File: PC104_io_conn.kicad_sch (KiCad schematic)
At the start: 1 part, among them P14 Conn_04x26_Pin

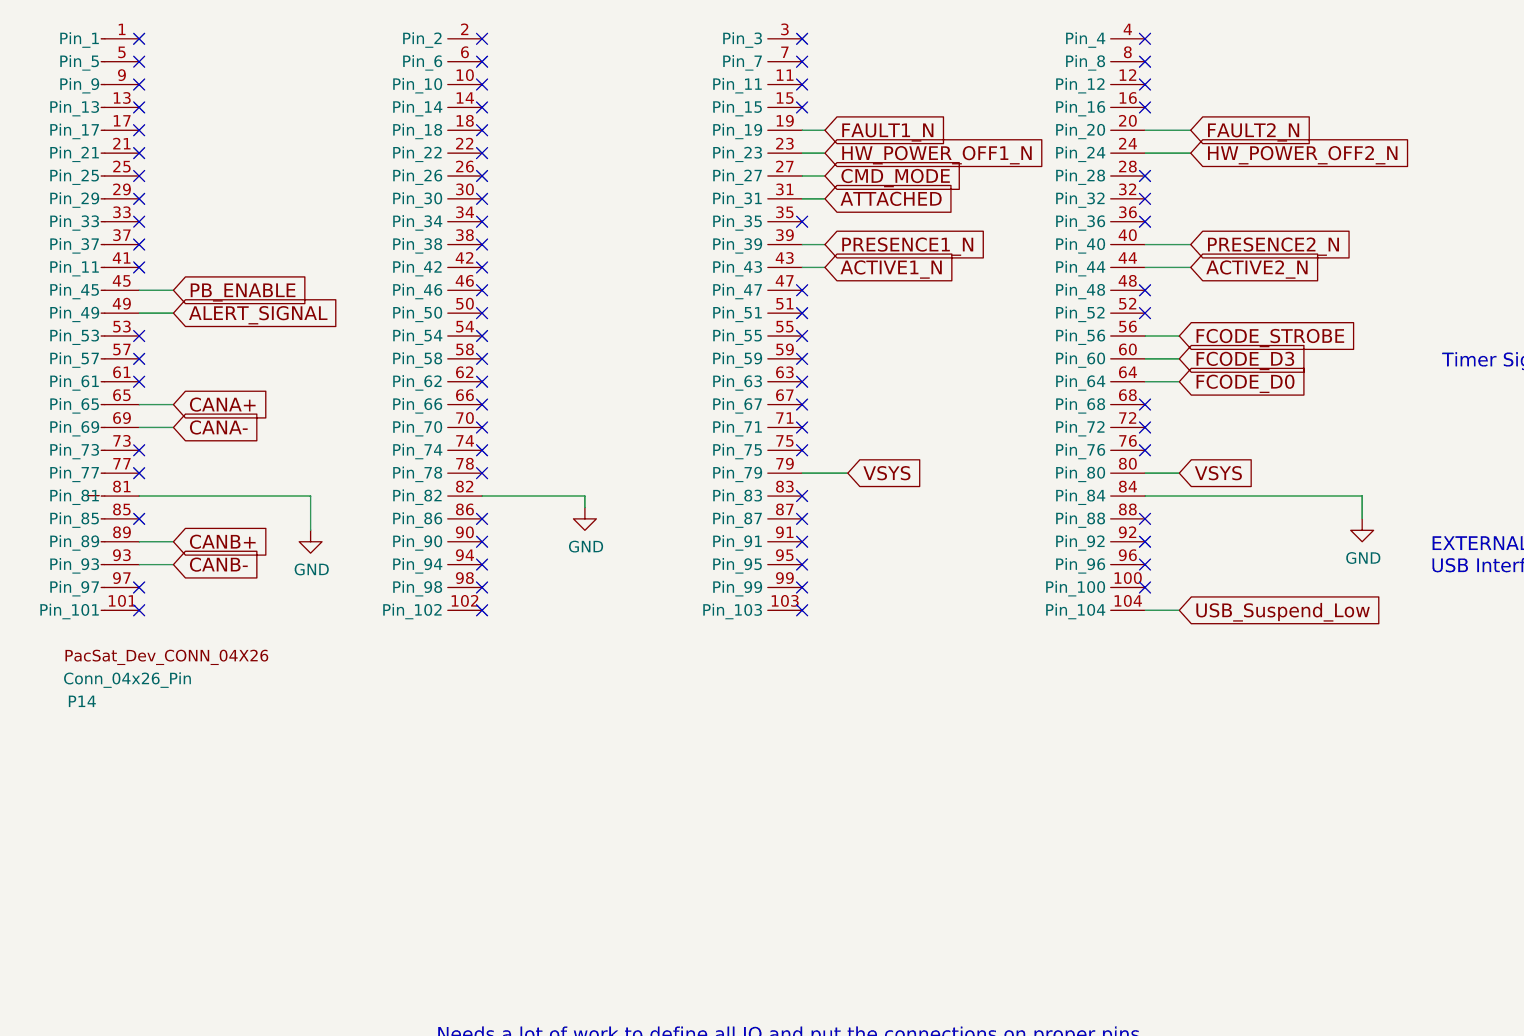
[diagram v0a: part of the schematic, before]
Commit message: Do a ton of work to switch to the CubeSat Kit Bus
Redo the connector, board shape, etc.

Signed-off-by: Corey Minyard <corey@minyard.net>
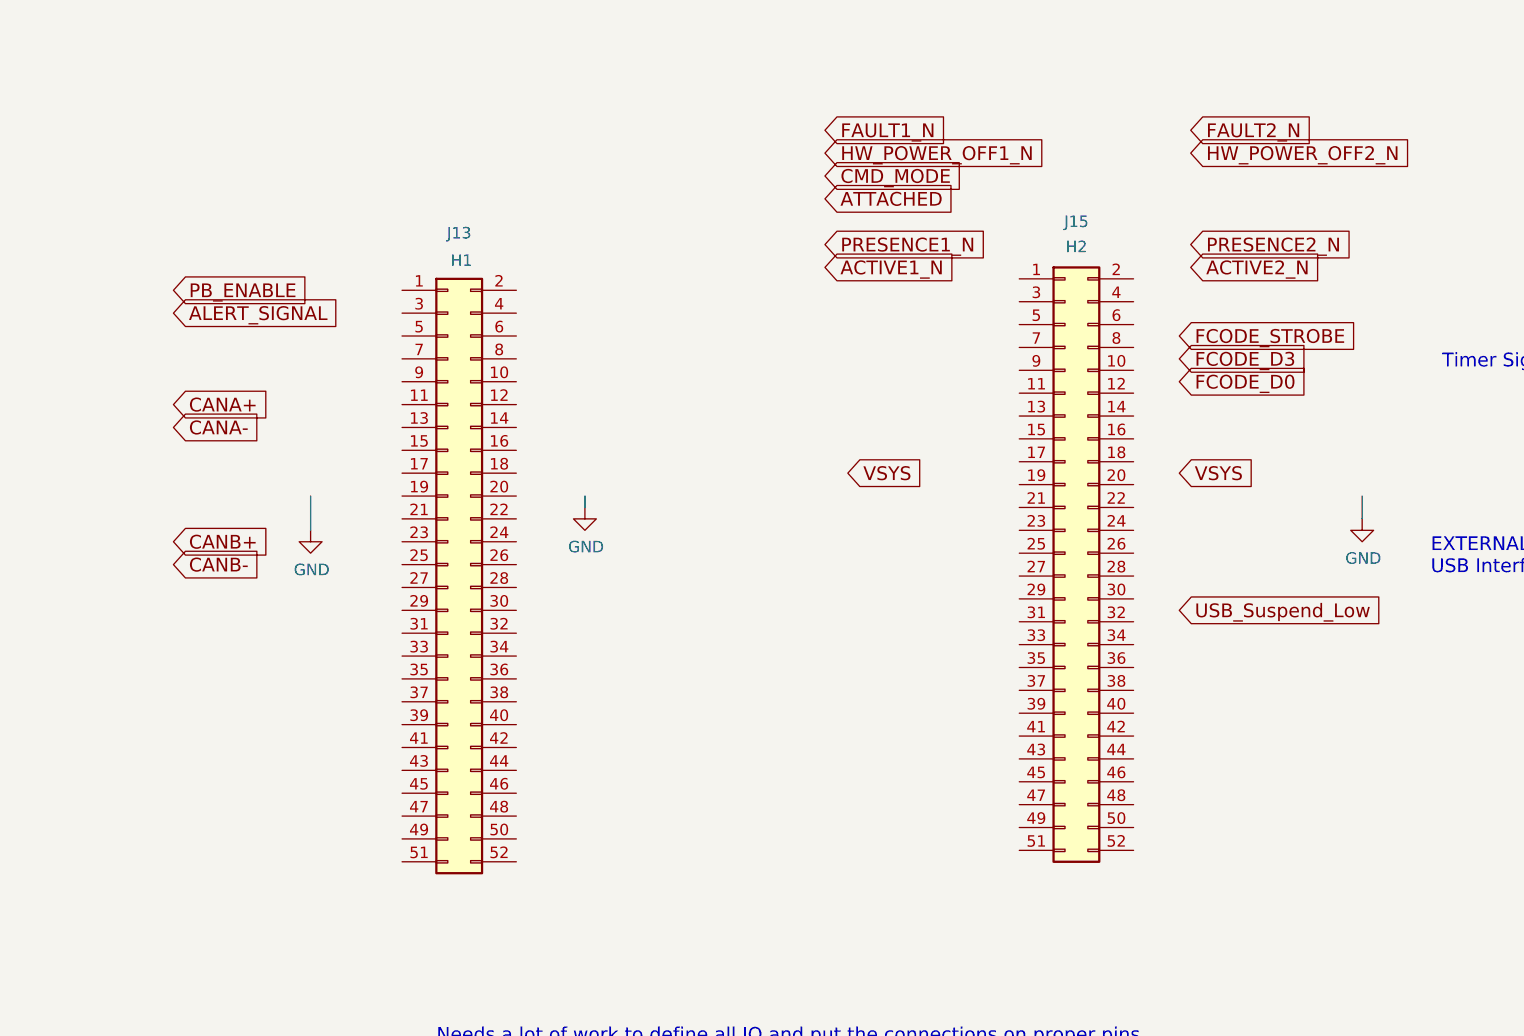
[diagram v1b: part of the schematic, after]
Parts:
- removed P14: Conn_04x26_Pin, PacSatDev_misc:PacSat_Dev_4_26, symbol PACSAT_DEV_misc:Conn_PC104
- added J13, J15: Conn_02x26_Odd_Even, PacSatDev_misc:CONN_ESQ-126-39-G-D_SAI, symbol Connector_Generic:Conn_02x26_Odd_Even
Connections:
- no-connect marks 79 -> 0

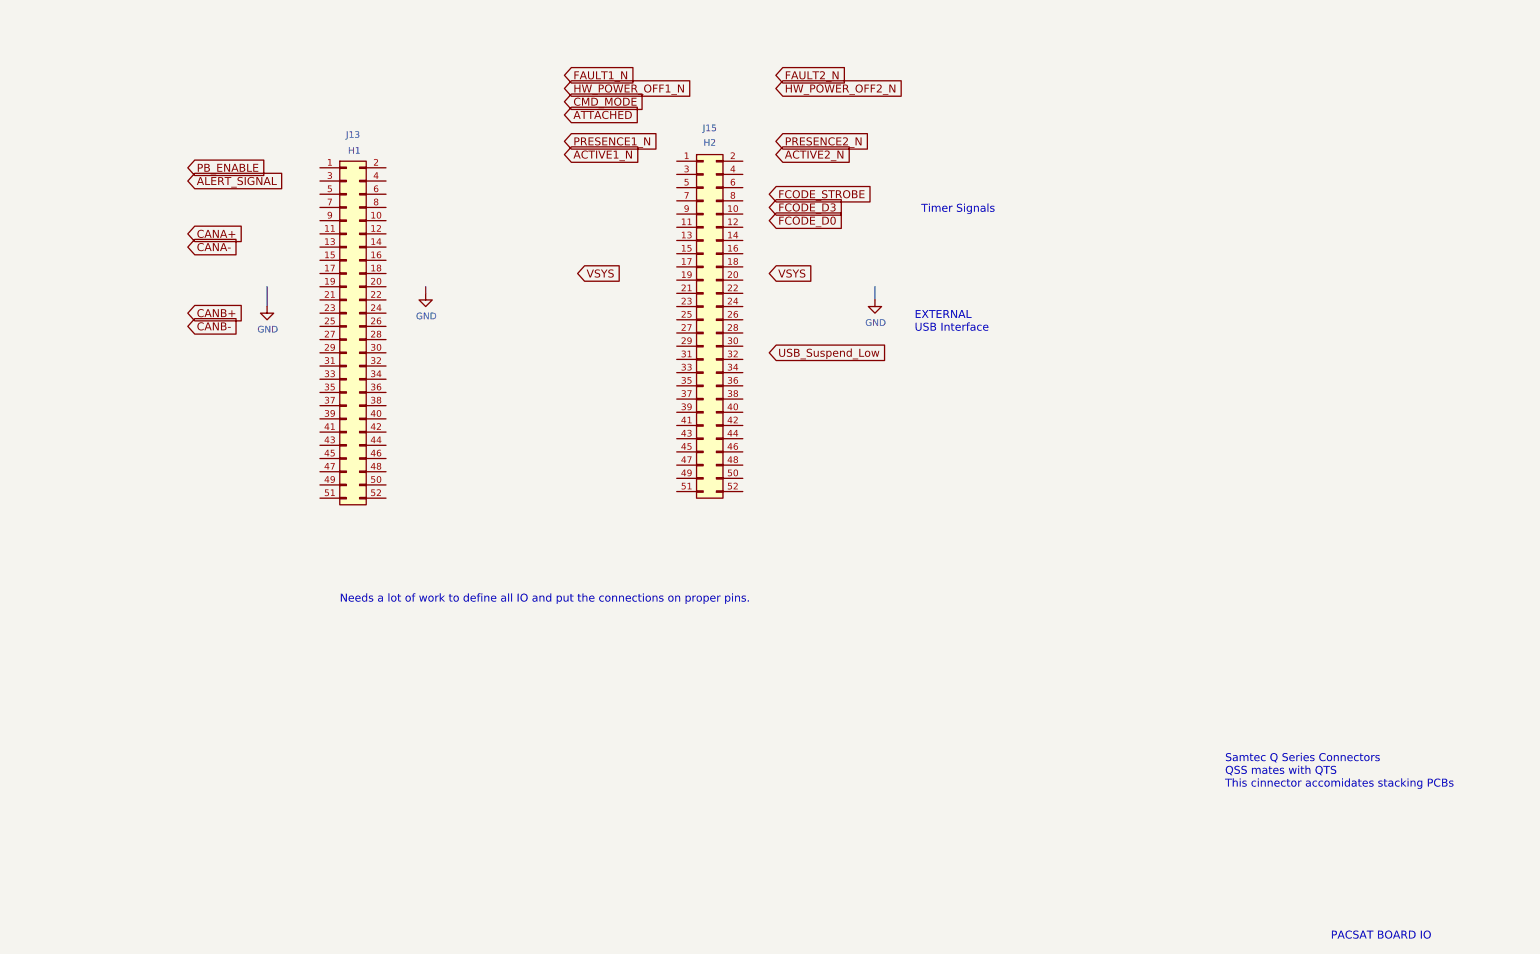
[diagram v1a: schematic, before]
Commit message: More work converting to the CubeSat Kit Bus
Signed-off-by: Corey Minyard <corey@minyard.net>
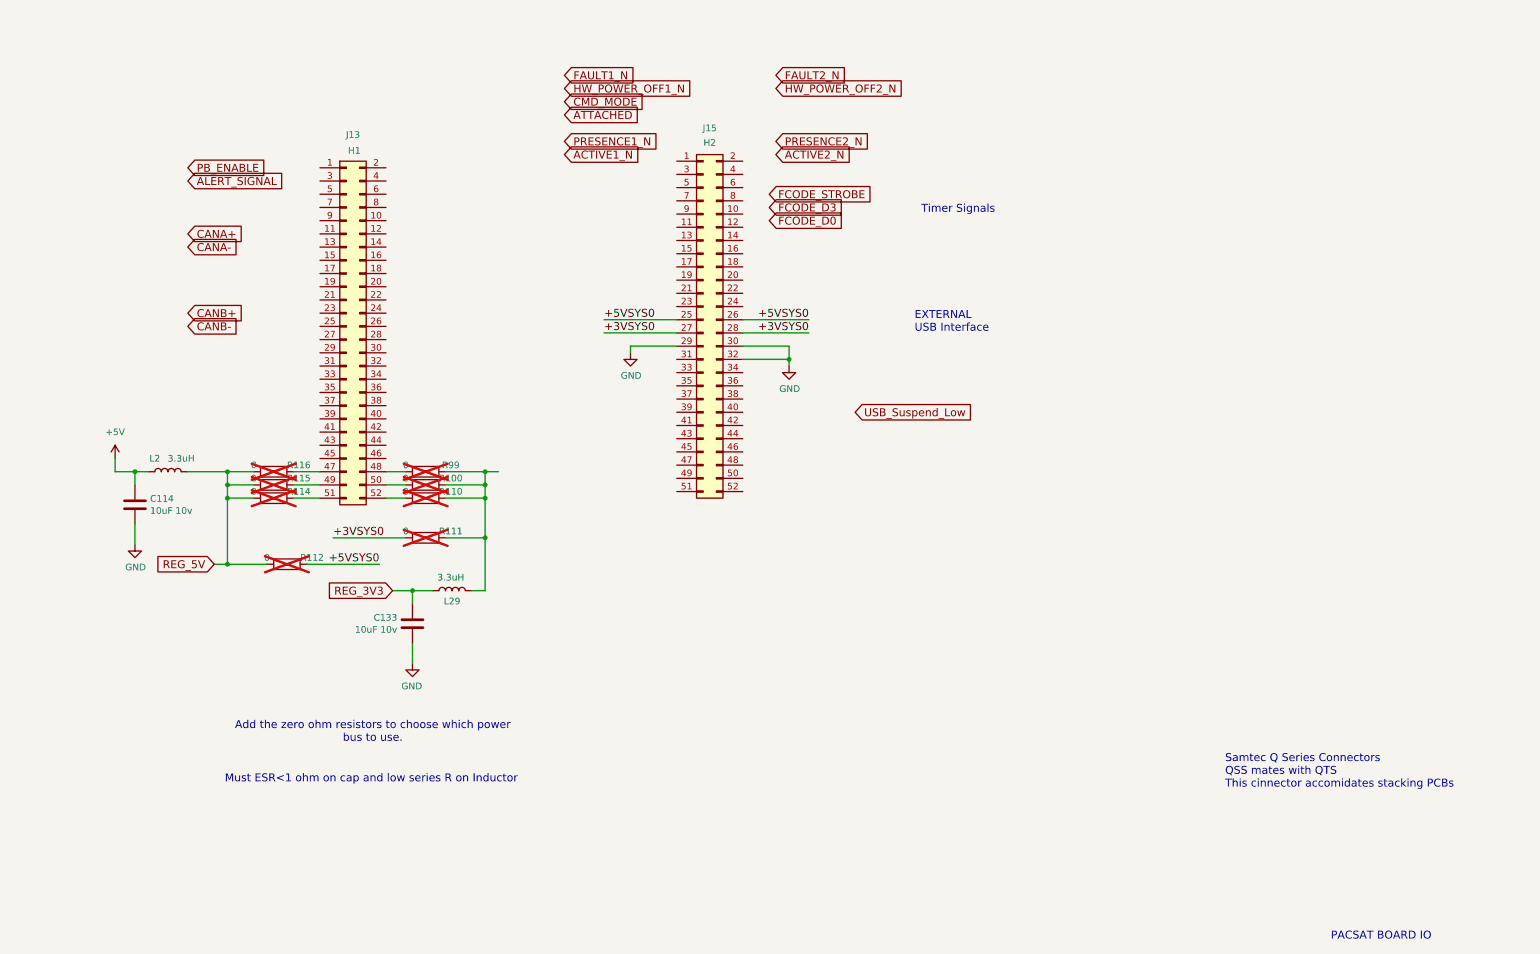
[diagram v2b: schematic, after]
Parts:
- added C114, C133: 10uF 10v, Capacitor_SMD:C_1206_3216Metric, symbol Device:C
- added L2, L29: 3.3uH, Inductor_SMD:L_1210_3225Metric_Pad1.42x2.65mm_HandSolder, symbol Device:L
- added R100, R110, R111, R112, R114, R115, R116, R99: 0, Resistor_SMD:R_0603_1608Metric_Pad0.98x0.95mm_HandSolder, symbol Device:R
- J13, J15: value Conn_02x26_Odd_Even -> ESQ-126-39-G-D_SAI
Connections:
- net GND: now also J15.29 (Pin_29), J15.30 (Pin_30), J15.32 (Pin_32), C114.2, C133.2
- net at J13.47 (Pin_47): now also R116.2
- net at J13.48 (Pin_48): now also R99.1
- net at J13.49 (Pin_49): now also R115.2
- net at J13.50 (Pin_50): now also R100.1
- net at J13.51 (Pin_51): now also R114.2
- net at J13.52 (Pin_52): now also R110.1
- net +5VSYS0: now reaches J15.25 (Pin_25)
- net +5VSYS0: now also J15.26 (Pin_26), R112.2
- net +3VSYS0: now reaches J15.27 (Pin_27)
- net +3VSYS0: now also J15.28 (Pin_28), R111.1
- new net: L29.1, R100.2, R110.2, R111.2, R99.2
- new net +5V: C114.1, L2.1
- new net REG_3V3: C133.1, L29.2
- new net REG_5V: L2.2, R112.1, R114.1, R115.1, R116.1
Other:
- note added: "Add the zero ohm resistors to choose which power bus to use."
- note added: "Must ESR<1 ohm on cap and low series R on Inductor"
- note removed: "Needs a lot of work to define all IO and put the connections on proper pins."

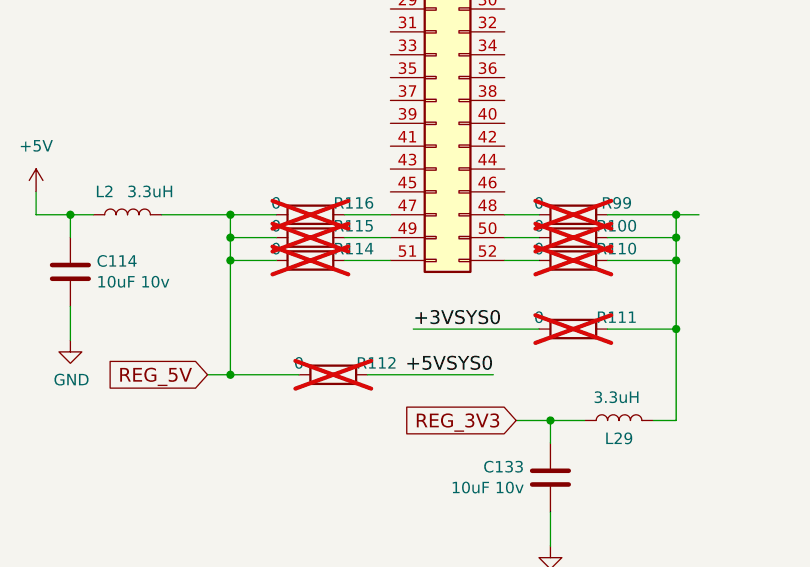
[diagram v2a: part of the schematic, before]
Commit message: Have the BOM file fixer output xls, not csv
The omega symbol gets translated properly from xls.

Signed-off-by: Corey Minyard <corey@minyard.net>
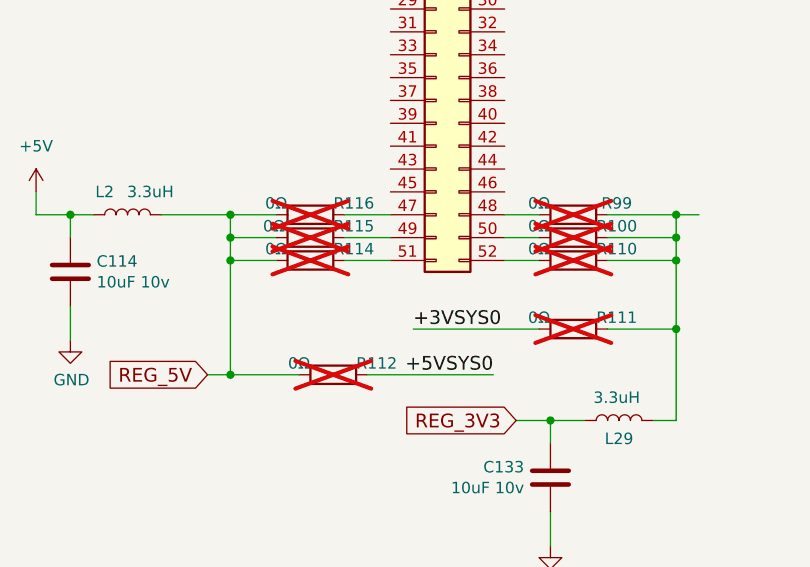
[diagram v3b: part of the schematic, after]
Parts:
- R100, R110, R111, R112, R114, R116, R99: value 0 -> 0Ω
- R115: value 0 -> 0Ω'
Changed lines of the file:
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@@
 			)
 		)
-		(property "Value" "0"
+		(property "Value" "0Ω"
 			(at 154.94 153.67 90)
 			(effects
@@
 			)
 		)
-		(property "Value" "0"
+		(property "Value" "0Ω"
 			(at 154.94 166.37 90)
 			(effects
@@
 			)
 		)
-		(property "Value" "0"
+		(property "Value" "0Ω'"
 			(at 125.73 156.21 90)
 			(effects
@@
 			)
 		)
-		(property "Value" "0"
+		(property "Value" "0Ω"
 			(at 125.73 153.67 90)
 			(effects
@@
 			)
 		)
-		(property "Value" "0"
+		(property "Value" "0Ω"
 			(at 128.27 171.45 90)
 			(effects
@@
 			)
 		)
-		(property "Value" "0"
+		(property "Value" "0Ω"
 			(at 125.73 158.75 90)
 			(effects
@@
 			)
 		)
-		(property "Value" "0"
+		(property "Value" "0Ω"
 			(at 154.94 158.75 90)
 			(effects
@@
 			)
 		)
-		(property "Value" "0"
+		(property "Value" "0Ω"
 			(at 154.94 156.21 90)
 			(effects
